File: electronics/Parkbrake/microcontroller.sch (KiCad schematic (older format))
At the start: 21 parts, among them U24 CAT250_EEPROM, U25 STM32F373RBTx, Y1 24Mhz

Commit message: More fixes and chenged components eat less boardspace
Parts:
- C43: footprint (none) -> Capacitors_SMD:C_0805
- C46: footprint Capacitors_SMD:c_elec_4x5.3 -> myfootprints:CP_0805; farnell 2068670 -> 2491429; part EDK475M035A9BAA -> TMCP0J475KTRF
- C48: footprint (none) -> Capacitors_SMD:C_0805; farnell (none) -> 2496940
- JP1: footprint (none) -> Resistors_SMD:R_0805_HandSoldering; farnell (none) -> 9240276; part (none) -> RC1206JR-070RL
- U24: value CAT250_EEPROM -> CAT25160_EEPROM
- Y1: footprint Crystals:Crystal_HC49-SD_SMD -> Crystals:ABM3; farnell 2467732 -> 2467794; part ABLS2-24.000MHZ-D4YF-T -> ABM3-24.000MHZ-D2Y-T
- renumbered R88 to R86, R89 to R87
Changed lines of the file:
@@
 F 0 "C48" H 8150 6275 50  0000 L CNN
 F 1 "100n" H 8150 6075 50  0000 L CNN
-F 2 "" H 8163 6025 50  0000 C CNN
+F 2 "Capacitors_SMD:C_0805" H 8163 6025 50  0001 C CNN
 F 3 "" H 8125 6175 50  0000 C CNN
 F 4 "0805B104J500CT" H 8125 6175 60  0001 C CNN "part"
+F 5 "2496940" H 8125 6175 60  0001 C CNN "farnell"
 	1    8125 6175
 	1    0    0    -1
@@
 F 0 "C46" H 7625 6275 50  0000 L CNN
 F 1 "4.7u" H 7625 6075 50  0000 L CNN
-F 2 "Capacitors_SMD:c_elec_4x5.3" H 7638 6025 50  0001 C CNN
+F 2 "myfootprints:CP_0805" H 7638 6025 50  0001 C CNN
 F 3 "" H 7600 6175 50  0000 C CNN
-F 4 "EDK475M035A9BAA" H 7600 6175 60  0001 C CNN "part"
-F 5 "2068670" H 7600 6175 60  0001 C CNN "farnell"
+F 4 "TMCP0J475KTRF" H 7600 6175 60  0001 C CNN "part"
+F 5 "2491429" H 7600 6175 60  0001 C CNN "farnell"
 	1    7600 6175
 	1    0    0    -1
@@
 $EndComp
 $Comp
-L GND #PWR073
+L GND #PWR70
 U 1 1 57915825
 P 7875 6325
-F 0 "#PWR073" H 7875 6075 50  0001 C CNN
+F 0 "#PWR70" H 7875 6075 50  0001 C CNN
 F 1 "GND" H 7875 6175 50  0001 C CNN
 F 2 "" H 7875 6325 50  0000 C CNN
@@
 $EndComp
 $Comp
-L GND #PWR074
+L GND #PWR71
 U 1 1 57915D33
 P 8925 6325
-F 0 "#PWR074" H 8925 6075 50  0001 C CNN
+F 0 "#PWR71" H 8925 6075 50  0001 C CNN
 F 1 "GND" H 8925 6175 50  0001 C CNN
 F 2 "" H 8925 6325 50  0000 C CNN
@@
 +3.3V
 $Comp
-L GND #PWR075
+L GND #PWR72
 U 1 1 57918611
 P 9700 6325
-F 0 "#PWR075" H 9700 6075 50  0001 C CNN
+F 0 "#PWR72" H 9700 6075 50  0001 C CNN
 F 1 "GND" H 9700 6175 50  0001 C CNN
 F 2 "" H 9700 6325 50  0000 C CNN
@@
 $EndComp
 $Comp
-L GND #PWR076
+L GND #PWR74
 U 1 1 57919116
 P 10975 6325
-F 0 "#PWR076" H 10975 6075 50  0001 C CNN
+F 0 "#PWR74" H 10975 6075 50  0001 C CNN
 F 1 "GND" H 10975 6175 50  0001 C CNN
 F 2 "" H 10975 6325 50  0000 C CNN
@@
 $EndComp
 $Comp
-L GND #PWR077
+L GND #PWR69
 U 1 1 5791A808
 P 6000 7525
-F 0 "#PWR077" H 6000 7275 50  0001 C CNN
+F 0 "#PWR69" H 6000 7275 50  0001 C CNN
 F 1 "GND" H 6000 7375 50  0001 C CNN
 F 2 "" H 6000 7525 50  0000 C CNN
@@
 F 0 "Y1" H 6200 7225 50  0000 C CNN
 F 1 "24Mhz" H 6200 6925 50  0000 C CNN
-F 2 "Crystals:Crystal_HC49-SD_SMD" H 6200 7075 50  0001 C CNN
+F 2 "Crystals:ABM3" H 6200 7075 50  0001 C CNN
 F 3 "" H 6200 7075 50  0000 C CNN
-F 4 "ABLS2-24.000MHZ-D4YF-T" H 6200 7075 60  0001 C CNN "part"
-F 5 "2467732" H 6200 7075 60  0001 C CNN "farnell"
+F 4 "ABM3-24.000MHZ-D2Y-T" H 6200 7075 60  0001 C CNN "part"
+F 5 "2467794" H 6200 7075 60  0001 C CNN "farnell"
 	1    6200 7075
 	1    0    0    -1
 $EndComp
 $Comp
-L R R89
+L R R87
 U 1 1 5791AD48
 P 6400 6925
-F 0 "R89" V 6480 6925 50  0000 C CNN
+F 0 "R87" V 6480 6925 50  0000 C CNN
 F 1 "255" V 6400 6925 50  0000 C CNN
 F 2 "Resistors_SMD:R_0805" V 6330 6925 50  0001 C CNN
@@
 OSC_OUT
 $Comp
-L R R88
+L R R86
 U 1 1 5791C2AA
 P 2825 7075
-F 0 "R88" V 2905 7075 50  0000 C CNN
+F 0 "R86" V 2905 7075 50  0000 C CNN
 F 1 "10k" V 2825 7075 50  0000 C CNN
 F 2 "Resistors_SMD:R_0805" V 2755 7075 50  0001 C CNN
@@
 F 0 "JP1" H 2825 7405 50  0000 C CNN
 F 1 "Jumper_NO_Small" H 2835 7265 50  0001 C CNN
-F 2 "" H 2825 7325 50  0000 C CNN
+F 2 "Resistors_SMD:R_0805_HandSoldering" H 2825 7325 50  0001 C CNN
 F 3 "" H 2825 7325 50  0000 C CNN
+F 4 "RC1206JR-070RL" H 2825 7325 60  0001 C CNN "part"
+F 5 "9240276" H 2825 7325 60  0001 C CNN "farnell"
 	1    2825 7325
 	0    -1   -1   0
@@
 	2900 7225 2825 7225
 $Comp
-L GND #PWR078
+L GND #PWR66
 U 1 1 5791C4BD
 P 2825 7425
-F 0 "#PWR078" H 2825 7175 50  0001 C CNN
+F 0 "#PWR66" H 2825 7175 50  0001 C CNN
 F 1 "GND" H 2825 7275 50  0001 C CNN
 F 2 "" H 2825 7425 50  0000 C CNN
@@
 P 4675 7200
 F 0 "U24" H 4375 7450 50  0000 L CNN
-F 1 "CAT250_EEPROM" H 4725 7450 50  0000 L CNN
+F 1 "CAT25160_EEPROM" H 4725 7450 50  0000 L CNN
 F 2 "Housings_SSOP:TSSOP-8_4.4x3mm_Pitch0.65mm" H 4325 7150 50  0001 C CNN
 F 3 "" H 4325 7150 50  0000 C CNN
@@
 F 0 "C43" H 4300 6825 50  0000 L CNN
 F 1 "1n" H 4300 6625 50  0000 L CNN
-F 2 "" H 4313 6575 50  0000 C CNN
+F 2 "Capacitors_SMD:C_0805" H 4313 6575 50  0001 C CNN
 F 3 "" H 4275 6725 50  0000 C CNN
 F 4 "GRM2165C1H102JA01D" H 4275 6725 60  0001 C CNN "part"
@@
 $EndComp
 $Comp
-L GND #PWR079
+L GND #PWR67
 U 1 1 579299FE
 P 4025 6875
-F 0 "#PWR079" H 4025 6625 50  0001 C CNN
+F 0 "#PWR67" H 4025 6625 50  0001 C CNN
 F 1 "GND" H 4025 6725 50  0001 C CNN
 F 2 "" H 4025 6875 50  0000 C CNN
@@
 +3.3V
 $Comp
-L GND #PWR080
+L GND #PWR68
 U 1 1 57929D36
 P 4675 7500
-F 0 "#PWR080" H 4675 7250 50  0001 C CNN
+F 0 "#PWR68" H 4675 7250 50  0001 C CNN
 F 1 "GND" H 4675 7350 50  0001 C CNN
 F 2 "" H 4675 7500 50  0000 C CNN
@@
 $EndComp
 $Comp
-L GND #PWR081
+L GND #PWR73
 U 1 1 579360FB
 P 10350 6325
-F 0 "#PWR081" H 10350 6075 50  0001 C CNN
+F 0 "#PWR73" H 10350 6075 50  0001 C CNN
 F 1 "GND" H 10350 6175 50  0001 C CNN
 F 2 "" H 10350 6325 50  0000 C CNN

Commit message: More work on inputs and 5 volt
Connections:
- net 3.3V is gone; now on net +3.3V: R86.1
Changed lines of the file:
@@
 $EndComp
 Text GLabel 2825 6925 1    60   Input ~ 0
-3.3V
++3.3V
 $Sheet
 S 700  7100 1625 500

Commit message: traceroute finished although there probably is some errors
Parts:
- JP1: value Jumper_NO_Small -> BOOT0
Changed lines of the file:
@@
 $EndComp
 $Comp
-L GND #PWR077
+L GND #PWR076
 U 1 1 57915825
 P 7875 6325
-F 0 "#PWR077" H 7875 6075 50  0001 C CNN
+F 0 "#PWR076" H 7875 6075 50  0001 C CNN
 F 1 "GND" H 7875 6175 50  0001 C CNN
 F 2 "" H 7875 6325 50  0000 C CNN
@@
 $EndComp
 $Comp
-L GND #PWR078
+L GND #PWR077
 U 1 1 57915D33
 P 8925 6325
-F 0 "#PWR078" H 8925 6075 50  0001 C CNN
+F 0 "#PWR077" H 8925 6075 50  0001 C CNN
 F 1 "GND" H 8925 6175 50  0001 C CNN
 F 2 "" H 8925 6325 50  0000 C CNN
@@
 +3.3V
 $Comp
-L GND #PWR079
+L GND #PWR078
 U 1 1 57918611
 P 9700 6325
-F 0 "#PWR079" H 9700 6075 50  0001 C CNN
+F 0 "#PWR078" H 9700 6075 50  0001 C CNN
 F 1 "GND" H 9700 6175 50  0001 C CNN
 F 2 "" H 9700 6325 50  0000 C CNN
@@
 $EndComp
 $Comp
-L GND #PWR080
+L GND #PWR079
 U 1 1 57919116
 P 10975 6325
-F 0 "#PWR080" H 10975 6075 50  0001 C CNN
+F 0 "#PWR079" H 10975 6075 50  0001 C CNN
 F 1 "GND" H 10975 6175 50  0001 C CNN
 F 2 "" H 10975 6325 50  0000 C CNN
@@
 $EndComp
 $Comp
-L GND #PWR081
+L GND #PWR080
 U 1 1 5791A808
 P 6000 7525
-F 0 "#PWR081" H 6000 7275 50  0001 C CNN
+F 0 "#PWR080" H 6000 7275 50  0001 C CNN
 F 1 "GND" H 6000 7375 50  0001 C CNN
 F 2 "" H 6000 7525 50  0000 C CNN
@@
 P 2825 7325
 F 0 "JP1" H 2825 7405 50  0000 C CNN
-F 1 "Jumper_NO_Small" H 2835 7265 50  0001 C CNN
+F 1 "BOOT0" H 2835 7265 50  0001 C CNN
 F 2 "Resistors_SMD:R_0805_HandSoldering" H 2825 7325 50  0001 C CNN
 F 3 "" H 2825 7325 50  0000 C CNN
@@
 	2900 7225 2825 7225
 $Comp
-L GND #PWR082
+L GND #PWR081
 U 1 1 5791C4BD
 P 2825 7425
-F 0 "#PWR082" H 2825 7175 50  0001 C CNN
+F 0 "#PWR081" H 2825 7175 50  0001 C CNN
 F 1 "GND" H 2825 7275 50  0001 C CNN
 F 2 "" H 2825 7425 50  0000 C CNN
@@
 $EndComp
 $Comp
-L GND #PWR083
+L GND #PWR082
 U 1 1 579299FE
 P 4025 6875
-F 0 "#PWR083" H 4025 6625 50  0001 C CNN
+F 0 "#PWR082" H 4025 6625 50  0001 C CNN
 F 1 "GND" H 4025 6725 50  0001 C CNN
 F 2 "" H 4025 6875 50  0000 C CNN
@@
 +3.3V
 $Comp
-L GND #PWR084
+L GND #PWR083
 U 1 1 57929D36
 P 4675 7500
-F 0 "#PWR084" H 4675 7250 50  0001 C CNN
+F 0 "#PWR083" H 4675 7250 50  0001 C CNN
 F 1 "GND" H 4675 7350 50  0001 C CNN
 F 2 "" H 4675 7500 50  0000 C CNN
@@
 $EndComp
 $Comp
-L GND #PWR085
+L GND #PWR084
 U 1 1 579360FB
 P 10350 6325
-F 0 "#PWR085" H 10350 6075 50  0001 C CNN
+F 0 "#PWR084" H 10350 6075 50  0001 C CNN
 F 1 "GND" H 10350 6175 50  0001 C CNN
 F 2 "" H 10350 6325 50  0000 C CNN

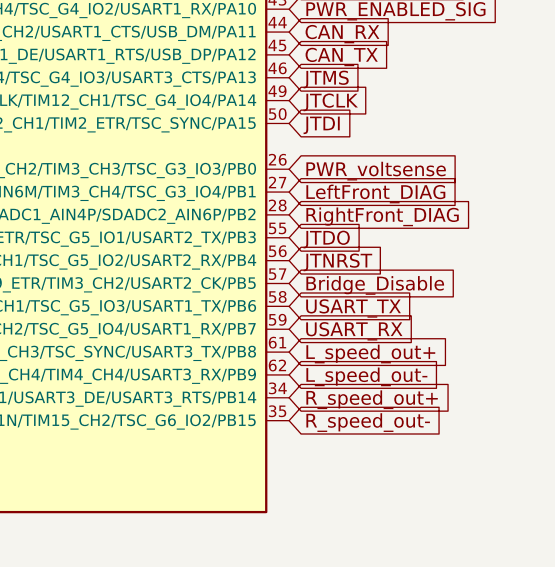
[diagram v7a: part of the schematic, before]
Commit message: Rethink hardware current limit, it didn't work as I rememberd
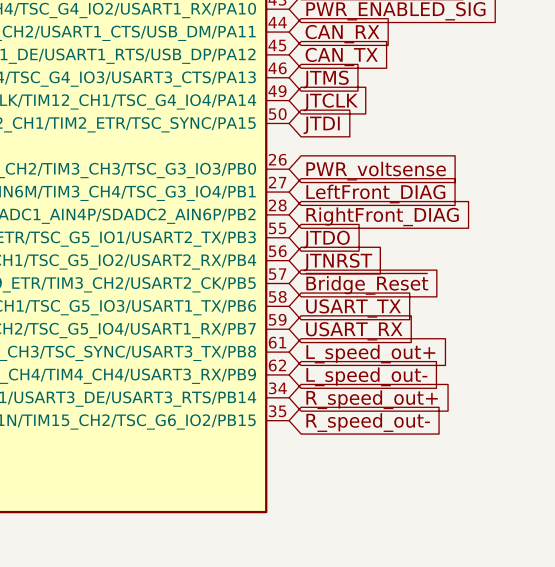
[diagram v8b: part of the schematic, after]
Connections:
- net Bridge_Disable renamed ~Bridge_Reset
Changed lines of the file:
@@
 RightRear_Loosen
 Text GLabel 10375 4100 2    60   Input ~ 0
-Bridge_Disable
+~Bridge_Reset
 Text GLabel 10375 2300 2    60   Input ~ 0
 LR_speed_in
